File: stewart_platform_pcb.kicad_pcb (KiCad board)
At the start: 2 copper layers, 1 part, among them U1 ESP32-S3-DevKitC

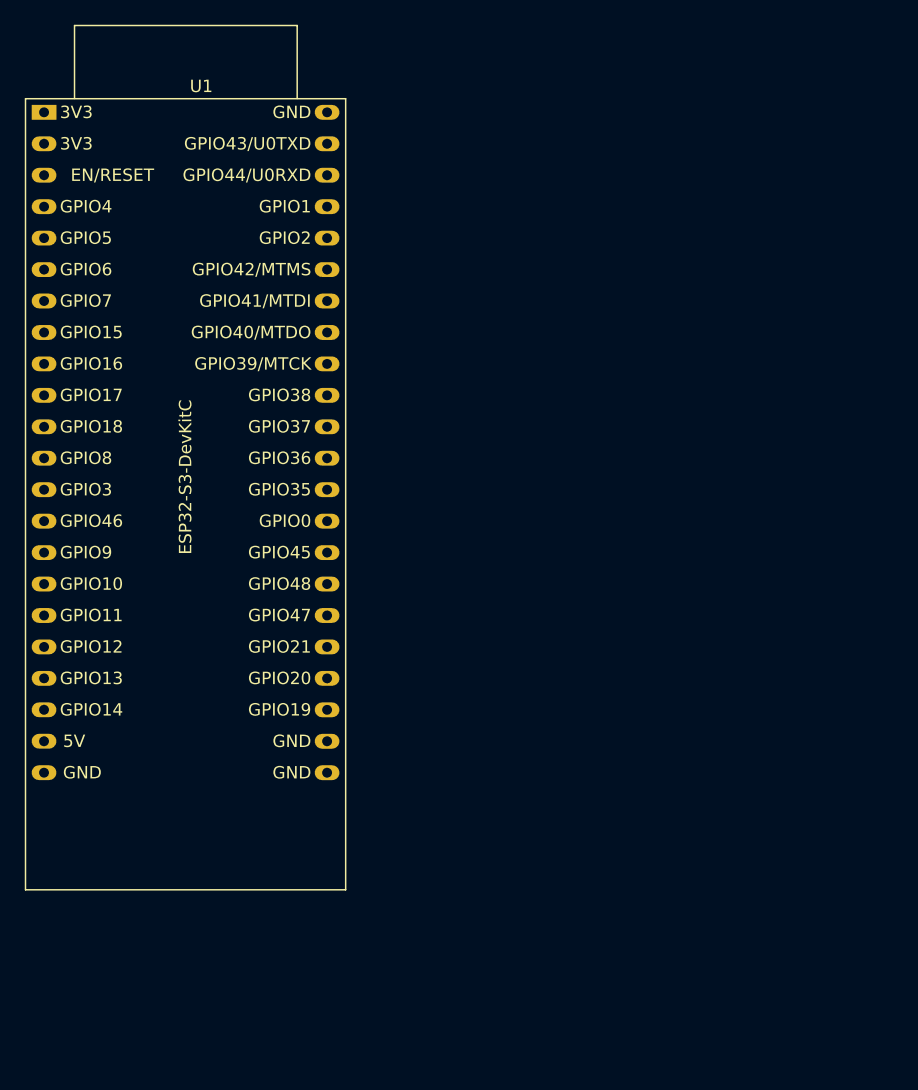
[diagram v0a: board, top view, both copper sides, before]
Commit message: Adding stepper drivers if needed/wanted. A4988 or TMC2209/TMC2208 compatible.
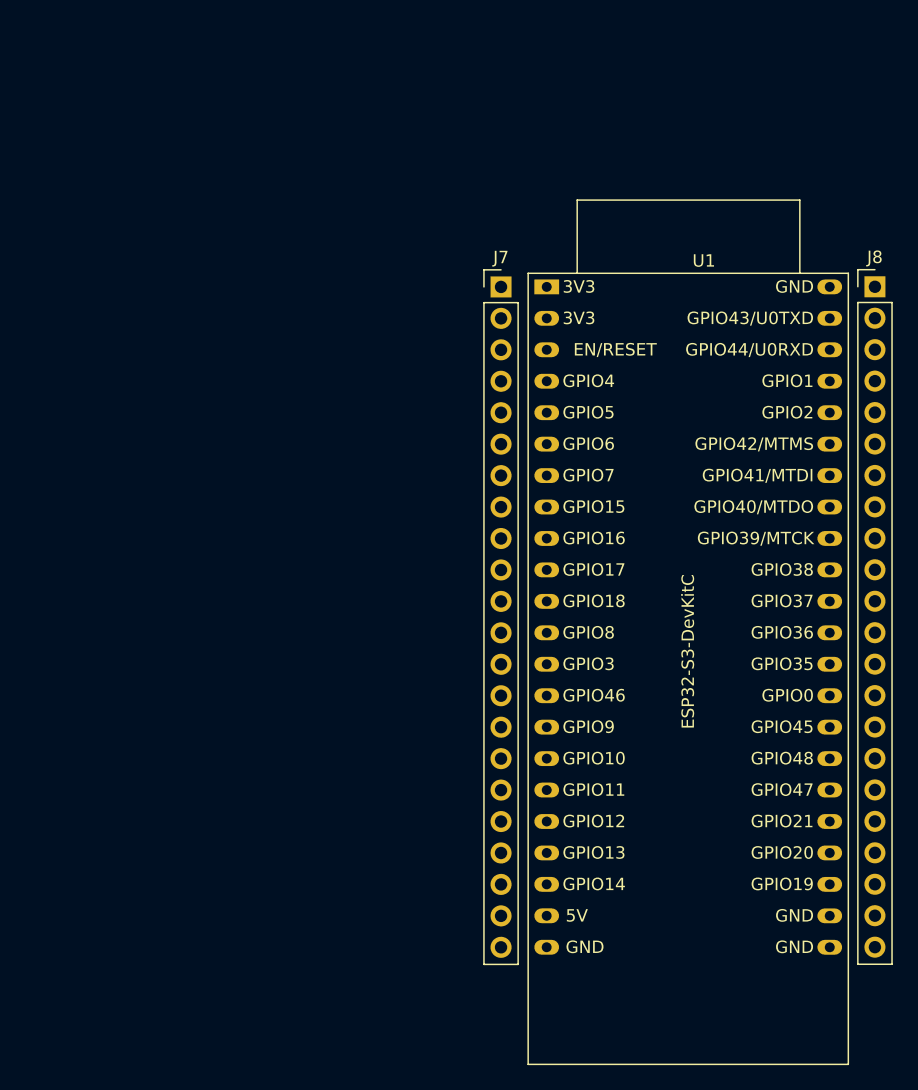
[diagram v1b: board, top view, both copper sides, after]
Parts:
- added J7: Conn_01x22, Connector_PinHeader_2.54mm:PinHeader_1x22_P2.54mm_Vertical, F.Cu at (129.8, 46.5)
- added J8: Conn_01x22, Connector_PinHeader_2.54mm:PinHeader_1x22_P2.54mm_Vertical, F.Cu at (160.0, 46.5)
- moved U1 43.0 mm to (133.5, 46.5)
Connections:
- net Net-(U1-GND-Pad22) renamed GND
- U1 pad 10: unconnected-(U1-GPIO17/ADC2_CH6-Pad10) -> /GPIO17
- U1 pad 11: unconnected-(U1-GPIO18/ADC2_CH7-Pad11) -> /GPIO18
- U1 pad 12: unconnected-(U1-GPIO8/ADC1_CH7-Pad12) -> /GPIO8
- U1 pad 13: unconnected-(U1-GPIO3/ADC1_CH2-Pad13) -> /GPIO3
- U1 pad 14: unconnected-(U1-GPIO46-Pad14) -> /GPIO46
- U1 pad 15: unconnected-(U1-GPIO9/ADC1_CH8-Pad15) -> /GPIO9
- U1 pad 16: unconnected-(U1-GPIO10/ADC1_CH9-Pad16) -> /GPIO10
- U1 pad 17: unconnected-(U1-GPIO11/ADC2_CH0-Pad17) -> /GPIO11
- U1 pad 18: unconnected-(U1-GPIO12/ADC2_CH1-Pad18) -> /GPIO12
- U1 pad 19: unconnected-(U1-GPIO13/ADC2_CH2-Pad19) -> /GPIO13
- U1 pad 20: unconnected-(U1-GPIO14/ADC2_CH3-Pad20) -> /GPIO14
- U1 pad 25: unconnected-(U1-GPIO19/USB_D--Pad25) -> /GPIO19
- U1 pad 26: unconnected-(U1-GPIO20/USB_D+-Pad26) -> /GPIO20
- U1 pad 27: unconnected-(U1-GPIO21-Pad27) -> /GPIO21
- U1 pad 28: unconnected-(U1-GPIO47-Pad28) -> /GPIO47
- U1 pad 29: unconnected-(U1-GPIO48-Pad29) -> /GPIO48
- U1 pad 3: unconnected-(U1-CHIP_PU-Pad3) -> /EN/RESET
- U1 pad 30: unconnected-(U1-GPIO45-Pad30) -> /GPIO45
- U1 pad 31: unconnected-(U1-GPIO0-Pad31) -> /GPIO0
- U1 pad 32: unconnected-(U1-GPIO35-Pad32) -> /GPIO35
- U1 pad 33: unconnected-(U1-GPIO36-Pad33) -> /GPIO36
- U1 pad 34: unconnected-(U1-GPIO37-Pad34) -> /GPIO37
- U1 pad 35: unconnected-(U1-GPIO38-Pad35) -> /GPIO38
- U1 pad 36: unconnected-(U1-GPIO39/MTCK-Pad36) -> /GPIO39/MTCK
- U1 pad 37: unconnected-(U1-GPIO40/MTDO-Pad37) -> /GPIO40/MTDO
- U1 pad 38: unconnected-(U1-GPIO41/MTDI-Pad38) -> /GPIO41/MTDI
- U1 pad 39: unconnected-(U1-GPIO42/MTMS-Pad39) -> /GPIO42/MTMS
- U1 pad 4: unconnected-(U1-GPIO4/ADC1_CH3-Pad4) -> /GPIO4
- U1 pad 40: unconnected-(U1-GPIO2/ADC1_CH1-Pad40) -> /GPIO2
- U1 pad 41: unconnected-(U1-GPIO1/ADC1_CH0-Pad41) -> /GPIO1
- U1 pad 42: unconnected-(U1-GPIO44/U0RXD-Pad42) -> /GPIO44/U0RXD
- U1 pad 43: unconnected-(U1-GPIO43/U0TXD-Pad43) -> /GPIO43/U0TXD
- U1 pad 5: unconnected-(U1-GPIO5/ADC1_CH4-Pad5) -> /GPIO5
- U1 pad 6: unconnected-(U1-GPIO6/ADC1_CH5-Pad6) -> /GPIO6
- U1 pad 7: unconnected-(U1-GPIO7/ADC1_CH6-Pad7) -> /GPIO7
- U1 pad 8: unconnected-(U1-GPIO15/ADC2_CH4/32K_P-Pad8) -> /GPIO15
- U1 pad 9: unconnected-(U1-GPIO16/ADC2_CH5/32K_N-Pad9) -> /GPIO16

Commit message: Updates
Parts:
- added A1: Pololu_Breakout_A4988, Module:Pololu_Breakout-16_15.2x20.3mm, F.Cu at (122.6, 37.5)
- added A2: Pololu_Breakout_A4988, Module:Pololu_Breakout-16_15.2x20.3mm, F.Cu at (95.7, 37.5)
- added A3: Pololu_Breakout_A4988, Module:Pololu_Breakout-16_15.2x20.3mm, F.Cu at (191.0, 37.5)
- added A4: Pololu_Breakout_A4988, Module:Pololu_Breakout-16_15.2x20.3mm, F.Cu at (218.2, 37.5)
- added A5: Pololu_Breakout_A4988, Module:Pololu_Breakout-16_15.2x20.3mm, F.Cu at (46.3, 197.3)
- added A6: Pololu_Breakout_A4988, Module:Pololu_Breakout-16_15.2x20.3mm, F.Cu at (-41.5, 165.3)
- added C10: 100nF, Capacitor_THT:C_Disc_D4.3mm_W1.9mm_P5.00mm, F.Cu at (98.5, 42.0)
- added C11: 100nF, Capacitor_THT:C_Disc_D4.3mm_W1.9mm_P5.00mm, F.Cu at (197.4, 42.0)
- added C12: 220uF, Capacitor_THT:C_Radial_D10.0mm_H12.5mm_P5.00mm, F.Cu at (104.7, 28.5)
- added C13: 220uF, Capacitor_THT:C_Radial_D10.0mm_H12.5mm_P5.00mm, F.Cu at (77.7, 28.5)
- added C14: 220uF, Capacitor_THT:C_Radial_D10.0mm_H12.5mm_P5.00mm, F.Cu at (200.7, 28.0)
- added C15: 220uF, Capacitor_THT:C_Radial_D10.0mm_H12.5mm_P5.00mm, F.Cu at (173.2, 28.5)
- added C16: 220uF, Capacitor_THT:C_Radial_D10.0mm_H12.5mm_P5.00mm, F.Cu at (62.7, 254.3)
- added C17: 220uF, Capacitor_THT:C_Radial_D10.0mm_H12.5mm_P5.00mm, F.Cu at (62.7, 265.8)
- added C18: 100nF, Capacitor_THT:C_Disc_D4.3mm_W1.9mm_P5.00mm, F.Cu at (-11.7, 279.7)
- added C19: 100nF, Capacitor_THT:C_Disc_D4.3mm_W1.9mm_P5.00mm, F.Cu at (-11.7, 283.2)
- added C8: 100nF, Capacitor_THT:C_Disc_D4.3mm_W1.9mm_P5.00mm, F.Cu at (102.0, 42.0)
- added C9: 100nF, Capacitor_THT:C_Disc_D4.3mm_W1.9mm_P5.00mm, F.Cu at (193.9, 42.0)
- added H1: MountingHole, MountingHole:MountingHole_3.2mm_M3, F.Cu at (44.6, 221.1)
- added H2: MountingHole, MountingHole:MountingHole_3.2mm_M3, F.Cu at (44.6, 229.0)
- added H3: MountingHole, MountingHole:MountingHole_3.2mm_M3, F.Cu at (52.6, 221.1)
- added H4: MountingHole, MountingHole:MountingHole_3.2mm_M3, F.Cu at (52.6, 229.0)
- added H5: MountingHole, MountingHole:MountingHole_3.2mm_M3, F.Cu at (60.5, 221.1)
- added H6: MountingHole, MountingHole:MountingHole_3.2mm_M3, F.Cu at (60.5, 229.0)
- added J1: Conn_01x03, Connector_Molex:Molex_KK-254_AE-6410-03A_1x03_P2.54mm_Vertical, F.Cu at (72.2, 42.6)
- added J10: Fan Screw Terminal, TerminalBlock_Phoenix:TerminalBlock_Phoenix_MKDS-1,5-2_1x02_P5.00mm_Horizontal, F.Cu at (51.9, 291.9)
- added J11: Conn_01x02, Connector_Molex:Molex_KK-254_AE-6410-02A_1x02_P2.54mm_Vertical, F.Cu at (6.34, 288.9)
- added J12: Conn_01x04, Connector_Molex:Molex_KK-254_AE-6410-04A_1x04_P2.54mm_Vertical, F.Cu at (122.2, 32.0)
- added J13: Conn_01x04, Connector_Molex:Molex_KK-254_AE-6410-04A_1x04_P2.54mm_Vertical, F.Cu at (95.2, 32.0)
- added J14: Conn_01x04, Connector_Molex:Molex_KK-254_AE-6410-04A_1x04_P2.54mm_Vertical, F.Cu at (190.7, 24.5)
- added J15: Conn_01x04, Connector_Molex:Molex_KK-254_AE-6410-04A_1x04_P2.54mm_Vertical, F.Cu at (217.9, 32.0)
- added J16: Conn_01x04, Connector_Molex:Molex_KK-254_AE-6410-04A_1x04_P2.54mm_Vertical, F.Cu at (95.2, 24.5)
- added J17: Conn_01x04, Connector_Molex:Molex_KK-254_AE-6410-04A_1x04_P2.54mm_Vertical, F.Cu at (122.2, 24.5)
- added J18: Conn_01x04, Connector_Molex:Molex_KK-254_AE-6410-04A_1x04_P2.54mm_Vertical, F.Cu at (190.7, 32.0)
- added J19: Conn_01x04, Connector_Molex:Molex_KK-254_AE-6410-04A_1x04_P2.54mm_Vertical, F.Cu at (218.0, 24.5)
- added J2: Conn_01x03, Connector_Molex:Molex_KK-254_AE-6410-03A_1x03_P2.54mm_Vertical, F.Cu at (128.0, 37.5)
- added J20: Conn_01x04, Connector_Molex:Molex_KK-254_AE-6410-04A_1x04_P2.54mm_Vertical, F.Cu at (30.8, 221.0)
- added J21: Conn_01x04, Connector_Molex:Molex_KK-254_AE-6410-04A_1x04_P2.54mm_Vertical, F.Cu at (30.8, 228.9)
- added J22: Conn_01x04, Connector_Molex:Molex_KK-254_AE-6410-04A_1x04_P2.54mm_Vertical, F.Cu at (30.8, 236.7)
- added J23: Conn_01x04, Connector_Molex:Molex_KK-254_AE-6410-04A_1x04_P2.54mm_Vertical, F.Cu at (30.8, 244.6)
- added J24: Conn_01x02, Connector_Molex:Molex_KK-254_AE-6410-02A_1x02_P2.54mm_Vertical, F.Cu at (72.2, 49.5)
- added J25: Conn_01x02, Connector_Molex:Molex_KK-254_AE-6410-02A_1x02_P2.54mm_Vertical, F.Cu at (128.0, 46.5)
- added J26: Conn_01x02, Connector_Molex:Molex_KK-254_AE-6410-02A_1x02_P2.54mm_Vertical, F.Cu at (168.0, 49.0)
- added J27: Conn_01x02, Connector_Molex:Molex_KK-254_AE-6410-02A_1x02_P2.54mm_Vertical, F.Cu at (223.5, 46.5)
- added J28: Conn_01x02, Connector_Molex:Molex_KK-254_AE-6410-02A_1x02_P2.54mm_Vertical, F.Cu at (13.5, 296.7)
- added J29: Conn_01x02, Connector_Molex:Molex_KK-254_AE-6410-02A_1x02_P2.54mm_Vertical, F.Cu at (20.6, 296.7)
- added J3: Conn_01x03, Connector_Molex:Molex_KK-254_AE-6410-03A_1x03_P2.54mm_Vertical, F.Cu at (168.0, 42.6)
- added J30: Conn_01x06, Connector_Molex:Molex_KK-254_AE-6410-06A_1x06_P2.54mm_Vertical, F.Cu at (90.7, 64.5)
- added J31: Conn_01x06, Connector_Molex:Molex_KK-254_AE-6410-06A_1x06_P2.54mm_Vertical, F.Cu at (90.7, 57.5)
- added J32: Conn_01x06, Connector_Molex:Molex_KK-254_AE-6410-06A_1x06_P2.54mm_Vertical, F.Cu at (186.2, 64.5)
- added J33: Conn_01x06, Connector_Molex:Molex_KK-254_AE-6410-06A_1x06_P2.54mm_Vertical, F.Cu at (186.3, 57.5)
- added J34: Conn_01x06, Connector_Molex:Molex_KK-254_AE-6410-06A_1x06_P2.54mm_Vertical, F.Cu at (-10.9, 252.4)
- added J35: Conn_01x06, Connector_Molex:Molex_KK-254_AE-6410-06A_1x06_P2.54mm_Vertical, F.Cu at (-10.9, 260.3)
- added J4: Conn_01x03, Connector_Molex:Molex_KK-254_AE-6410-03A_1x03_P2.54mm_Vertical, F.Cu at (223.5, 37.5)
- added J5: Conn_01x03, Connector_Molex:Molex_KK-254_AE-6410-03A_1x03_P2.54mm_Vertical, F.Cu at (-20.6, 252.4)
- added J6: Conn_01x03, Connector_Molex:Molex_KK-254_AE-6410-03A_1x03_P2.54mm_Vertical, F.Cu at (-20.6, 260.3)
- added J9: Power Input, TerminalBlock_Phoenix:TerminalBlock_Phoenix_MKDS-1,5-2_1x02_P5.00mm_Horizontal, F.Cu at (39.9, 291.9)
- added R1: 10, Resistor_THT:R_Axial_DIN0207_L6.3mm_D2.5mm_P7.62mm_Horizontal, F.Cu at (73.5, 55.2)
- added R10: 1, Resistor_THT:R_Axial_DIN0207_L6.3mm_D2.5mm_P7.62mm_Horizontal, F.Cu at (16.4, 250.5)
- added R11: 10, Resistor_THT:R_Axial_DIN0207_L6.3mm_D2.5mm_P7.62mm_Horizontal, F.Cu at (16.4, 254.6)
- added R12: 1, Resistor_THT:R_Axial_DIN0207_L6.3mm_D2.5mm_P7.62mm_Horizontal, F.Cu at (16.4, 258.6)
- added R13: 22k, Resistor_THT:R_Axial_DIN0207_L6.3mm_D2.5mm_P7.62mm_Horizontal, F.Cu at (115.5, 66.0)
- added R14: 22k, Resistor_THT:R_Axial_DIN0207_L6.3mm_D2.5mm_P7.62mm_Horizontal, F.Cu at (115.5, 62.5)
- added R15: 22k, Resistor_THT:R_Axial_DIN0207_L6.3mm_D2.5mm_P7.62mm_Horizontal, F.Cu at (115.4, 55.5)
- added R16: 22k, Resistor_THT:R_Axial_DIN0207_L6.3mm_D2.5mm_P7.62mm_Horizontal, F.Cu at (115.5, 59.0)
- added R17: 22k, Resistor_THT:R_Axial_DIN0207_L6.3mm_D2.5mm_P7.62mm_Horizontal, F.Cu at (210.9, 66.5)
- added R18: 22k, Resistor_THT:R_Axial_DIN0207_L6.3mm_D2.5mm_P7.62mm_Horizontal, F.Cu at (210.9, 63.0)
- added R19: 22k, Resistor_THT:R_Axial_DIN0207_L6.3mm_D2.5mm_P7.62mm_Horizontal, F.Cu at (210.9, 56.0)
- added R2: 1, Resistor_THT:R_Axial_DIN0207_L6.3mm_D2.5mm_P7.62mm_Horizontal, F.Cu at (70.0, 62.8)
- added R20: 22k, Resistor_THT:R_Axial_DIN0207_L6.3mm_D2.5mm_P7.62mm_Horizontal, F.Cu at (210.9, 59.5)
- added R21: 22k, Resistor_THT:R_Axial_DIN0207_L6.3mm_D2.5mm_P7.62mm_Horizontal, F.Cu at (27.2, 258.6)
- added R22: 22k, Resistor_THT:R_Axial_DIN0207_L6.3mm_D2.5mm_P7.62mm_Horizontal, F.Cu at (27.2, 262.7)
- added R23: 22k, Resistor_THT:R_Axial_DIN0207_L6.3mm_D2.5mm_P7.62mm_Horizontal, F.Cu at (27.2, 266.7)
- added R24: 22k, Resistor_THT:R_Axial_DIN0207_L6.3mm_D2.5mm_P7.62mm_Horizontal, F.Cu at (27.2, 270.8)
- added R3: 10, Resistor_THT:R_Axial_DIN0207_L6.3mm_D2.5mm_P7.62mm_Horizontal, F.Cu at (126.5, 55.2)
- added R4: 1, Resistor_THT:R_Axial_DIN0207_L6.3mm_D2.5mm_P7.62mm_Horizontal, F.Cu at (130.0, 62.8)
- added R5: 10, Resistor_THT:R_Axial_DIN0207_L6.3mm_D2.5mm_P7.62mm_Horizontal, F.Cu at (190.7, 79.0)
- added R6: 1, Resistor_THT:R_Axial_DIN0207_L6.3mm_D2.5mm_P7.62mm_Horizontal, F.Cu at (190.7, 83.0)
- added R7: 10, Resistor_THT:R_Axial_DIN0207_L6.3mm_D2.5mm_P7.62mm_Horizontal, F.Cu at (190.7, 87.1)
- added R8: 1, Resistor_THT:R_Axial_DIN0207_L6.3mm_D2.5mm_P7.62mm_Horizontal, F.Cu at (190.7, 91.2)
- added R9: 10, Resistor_THT:R_Axial_DIN0207_L6.3mm_D2.5mm_P7.62mm_Horizontal, F.Cu at (5.62, 282.9)
- added SW1: SW_DIP_x04, Button_Switch_THT:SW_DIP_SPSTx04_Slide_9.78x12.34mm_W7.62mm_P2.54mm, F.Cu at (104.7, 57.0)
- added SW2: SW_DIP_x04, Button_Switch_THT:SW_DIP_SPSTx04_Slide_9.78x12.34mm_W7.62mm_P2.54mm, F.Cu at (200.4, 57.2)
- added SW3: SW_DIP_x04, Button_Switch_THT:SW_DIP_SPSTx04_Slide_9.78x12.34mm_W7.62mm_P2.54mm, F.Cu at (61.1, 274.8)
- moved J7 109.6 mm to (84.9, 146.4), turned to 90 degrees
- moved U1 107.8 mm to (84.8, 142.7), turned to 90 degrees
- moved J8 102.5 mm to (84.8, 116.2), turned to 90 degrees
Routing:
- net GND: track 0.00 -> 92.1 mm
- net /~ENABLE: track 0.00 -> 67.1 mm
- net /~SLEEP/CLK: track 0.00 -> 62.5 mm
- net +3V3: track 0.00 -> 55.8 mm
- net Net-(A3-MS1): track 0.00 -> 48.3 mm
- net /M0_STP: track 0.00 -> 47.4 mm
- net Net-(A2-MS1): track 0.00 -> 46.6 mm
- net /M0_DIR: track 0.00 -> 44.3 mm
- net Net-(A3-MS2): track 0.00 -> 42.8 mm
- net Net-(A2-MS2): track 0.00 -> 41.6 mm
- net +V_MOT: track 0.00 -> 36.7 mm
- net /MS3/SPRD/PDN_UART_0/NC: track 0.00 -> 30.3 mm
- net /~RESET/PDN_UART_1: track 0.00 -> 29.9 mm
- net /~RESET/PDN_UART_0: track 0.00 -> 29.1 mm
- net /MS3/SPRD/PDN_UART_1/NC: track 0.00 -> 29.1 mm
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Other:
- copper layers 2 -> 4

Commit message: Before rotations
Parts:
- added C1: 2.2uF, Capacitor_THT:C_Radial_D6.3mm_H5.0mm_P2.50mm, F.Cu at (94.2, 76.0)
- added C2: 2.2uF, Capacitor_THT:C_Radial_D6.3mm_H5.0mm_P2.50mm, F.Cu at (39.1, 76.0)
- added C3: 2.2uF, Capacitor_THT:C_Radial_D6.3mm_H5.0mm_P2.50mm, F.Cu at (169.8, 76.2)
- added C4: 2.2uF, Capacitor_THT:C_Radial_D6.3mm_H5.0mm_P2.50mm, F.Cu at (114.5, 76.5)
- added C5: 2.2uF, Capacitor_THT:C_Radial_D6.3mm_H5.0mm_P2.50mm, F.Cu at (250.9, 75.6)
- added C6: 2.2uF, Capacitor_THT:C_Radial_D6.3mm_H5.0mm_P2.50mm, F.Cu at (196.2, 75.8)
- J1, J2, J3, J4, J5, J6: footprint Connector_Molex:Molex_KK-254_AE-6410-03A_1x03_P2.54mm_Vertical -> Connector_JST:JST_XH_B3B-XH-A_1x03_P2.50mm_Vertical
- J11, J24, J25, J26, J27, J28, J29: footprint Connector_Molex:Molex_KK-254_AE-6410-02A_1x02_P2.54mm_Vertical -> Connector_JST:JST_XH_B2B-XH-A_1x02_P2.50mm_Vertical
- J12, J13, J14, J15, J16, J17, J18, J19, J20, J21, J22, J23: footprint Connector_Molex:Molex_KK-254_AE-6410-04A_1x04_P2.54mm_Vertical -> Connector_JST:JST_XH_B4B-XH-A_1x04_P2.50mm_Vertical
- J30, J31, J32, J33, J34, J35: footprint Connector_Molex:Molex_KK-254_AE-6410-06A_1x06_P2.54mm_Vertical -> Connector_JST:JST_XH_B6B-XH-A_1x06_P2.50mm_Vertical
- moved J11 392.4 mm to (301.5, 30.2)
- moved J10 360.3 mm to (324.8, 56.5)
- moved J9 360.3 mm to (312.7, 56.5)
- moved J5 340.0 mm to (251.8, 49.0), turned to 90 degrees
- moved J28 337.6 mm to (251.8, 57.5), turned to 90 degrees
- moved C19 334.9 mm to (226.2, 47.4), turned to 90 degrees
- moved H1 330.6 mm to (314.1, 29.6)
- moved H2 330.6 mm to (314.1, 37.5)
- moved H3 330.6 mm to (322.1, 29.6)
- moved H4 330.6 mm to (322.1, 37.5)
- moved H5 330.6 mm to (330.0, 29.6)
- moved H6 330.6 mm to (330.0, 37.5)
- moved C18 330.4 mm to (223.2, 47.4), turned to 90 degrees
- moved R9 329.0 mm to (250.5, 63.2), turned to -90 degrees
- moved J6 307.3 mm to (197.8, 44.0), turned to -90 degrees
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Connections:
- J32 pad 3: /M2_STP -> /M2_DIR
- J32 pad 5: /M2_DIR -> /M2_STP
- J33 pad 3: /M3_STP -> /M3_DIR
- J33 pad 5: /M3_DIR -> /M3_STP
- J34 pad 3: /M4_STP -> /M4_DIR
- J34 pad 5: /M4_DIR -> /M4_STP
- J35 pad 3: /M5_STP -> /M5_DIR
- J35 pad 5: /M5_DIR -> /M5_STP
- R1 pad 2: /GPIO35 -> /LIM_SW_0
- R10 pad 1: /GPIO47 -> /GPIO38
- R11 pad 2: /GPIO48 -> /GPIO47
- R12 pad 1: /GPIO48 -> /GPIO47
- R2 pad 1: /GPIO35 -> /LIM_SW_0
- R3 pad 2: /GPIO36 -> /GPIO35
- R4 pad 1: /GPIO36 -> /GPIO35
- R5 pad 2: /GPIO37 -> /GPIO36
- R6 pad 1: /GPIO37 -> /GPIO36
- R7 pad 2: /GPIO38 -> /GPIO37
- R8 pad 1: /GPIO38 -> /GPIO37
- R9 pad 2: /GPIO47 -> /GPIO38
- SW3 pad 1: unconnected-(SW3-Pad1) -> +3V3
- SW3 pad 2: unconnected-(SW3-Pad2) -> +3V3
- SW3 pad 3: unconnected-(SW3-Pad3) -> +3V3
- SW3 pad 4: unconnected-(SW3-Pad4) -> +3V3
- SW3 pad 5: Net-(A5-MS1) -> Net-(A6-MS1)
- SW3 pad 6: Net-(A5-MS2) -> Net-(A6-MS2)
- SW3 pad 7: Net-(A6-MS1) -> Net-(A5-MS1)
- SW3 pad 8: Net-(A6-MS2) -> Net-(A5-MS2)
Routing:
- net +V_MOT: track 36.7 -> 159.6 mm
- net GND: track 92.1 -> 152.8 mm
- net /~ENABLE: track 67.1 -> 124.2 mm
- net /M2_STP: track 0.00 -> 44.5 mm
- net /M4_STP: track 0.00 -> 44.0 mm
- net Net-(A6-MS1): track 0.00 -> 43.7 mm
- net /M2_DIR: track 0.00 -> 42.1 mm
- net /M4_DIR: track 0.00 -> 42.0 mm
- net Net-(A6-MS2): track 0.00 -> 38.8 mm
- net /~SLEEP/CLK: track 62.5 -> 91.0 mm
- net +3V3: track 55.8 -> 84.1 mm
- net Net-(J27-Pin_2): track 0.00 -> 21.0 mm
- net Net-(J26-Pin_2): track 0.00 -> 20.4 mm
- net Net-(J29-Pin_2): track 0.00 -> 19.3 mm
- net Net-(J28-Pin_2): track 0.00 -> 19.2 mm
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- added copper zone on F.Cu, net GND
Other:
- board text added: "LIM_SW_0"
- board text added: "LIM_SW_1"
- board text added: "LIM_SW_2"
- board text added: "LIM_SW_3"
- board text added: "LIM_SW_4"
- board text added: "LIM_SW_5"
- board text added: "M0"
- board text added: "M1"
- board text added: "M2"
- board text added: "M3"
- board text added: "M4"
- board text added: "M5"

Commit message: Arranging in circle
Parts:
- moved C15 228.9 mm to (296.1, 177.0), turned to -120 degrees
- moved J14 223.8 mm to (288.8, 194.7), turned to 60 degrees
- moved J19 218.9 mm to (276.0, 216.9), turned to 60 degrees
- moved C14 217.4 mm to (283.2, 199.3), turned to -120 degrees
- moved J10 216.6 mm to (181.0, 218.5)
- moved J4 210.0 mm to (286.4, 167.7), turned to 150 degrees
- moved J18 209.9 mm to (281.7, 190.6), turned to 60 degrees
- moved J15 204.6 mm to (268.9, 212.7), turned to 60 degrees
- moved J21 204.2 mm to (108.5, 179.1), turned to -60 degrees
- moved J9 201.7 mm to (192.5, 218.5)
- moved A3 199.7 mm to (276.3, 187.8), turned to 150 degrees
- moved J22 199.4 mm to (121.5, 201.6), turned to -60 degrees
- moved C16 198.3 mm to (132.8, 216.7), turned to 120 degrees
- moved C17 195.8 mm to (120.0, 194.7), turned to 120 degrees
- moved A4 194.2 mm to (262.7, 211.4), turned to 150 degrees
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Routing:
- removed copper zone on F.Cu, net GND

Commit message: Found working outline
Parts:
- moved H1 284.2 mm to (111.5, 233.1)
- moved H2 284.2 mm to (111.5, 241.0)
- moved H3 284.2 mm to (119.5, 233.1)
- moved H4 284.2 mm to (119.5, 241.0)
- moved H5 284.2 mm to (127.5, 233.1)
- moved H6 284.2 mm to (127.5, 241.0)
- moved J11 88.0 mm to (151.8, 245.5)
- moved J9 35.2 mm to (192.5, 253.7)
- moved J10 32.9 mm to (170.5, 249.7)
- moved C14 19.3 mm to (277.6, 180.9)
- moved C15 19.3 mm to (290.5, 158.6)
- moved J27 19.3 mm to (271.0, 143.7)
- moved R7 19.3 mm to (264.7, 137.2)
- moved J3 19.3 mm to (249.3, 193.8)
- moved J32 19.3 mm to (249.3, 152.5)
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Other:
- board outline added: 194 x 168 mm
